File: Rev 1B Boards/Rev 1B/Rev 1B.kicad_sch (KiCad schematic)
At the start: 32 parts, among them J1 JST4_F, J10 Conn_01x01_Pin, J11 Conn_01x01_Pin, J12 Conn_01x01_Pin, J13 Banana 2P, J14 Conn_01x01_Pin, J15 Banana 2P, J16 Conn_01x01_Pin, J17 Conn_01x01_Pin, J18 Banana 2P, J19 Banana 2P, J2 Banana 2P, J21 Banana 2P, J22 Banana 2P, J23 Banana 2P, J24 Banana 2P, J25 Banana 2P, J26 Banana 2P, J27 Banana 2P, J28 Banana 2P, J29 Banana 2P, J3 Banana 2P, J30 Banana 2P, J31 Banana 2P, J4 Banana 2P, J5 Banana 2P, J6 Banana 2P, J7 Conn_01x01_Pin, Q1 BSC059N04LS6, Q2 BSC059N04LS6

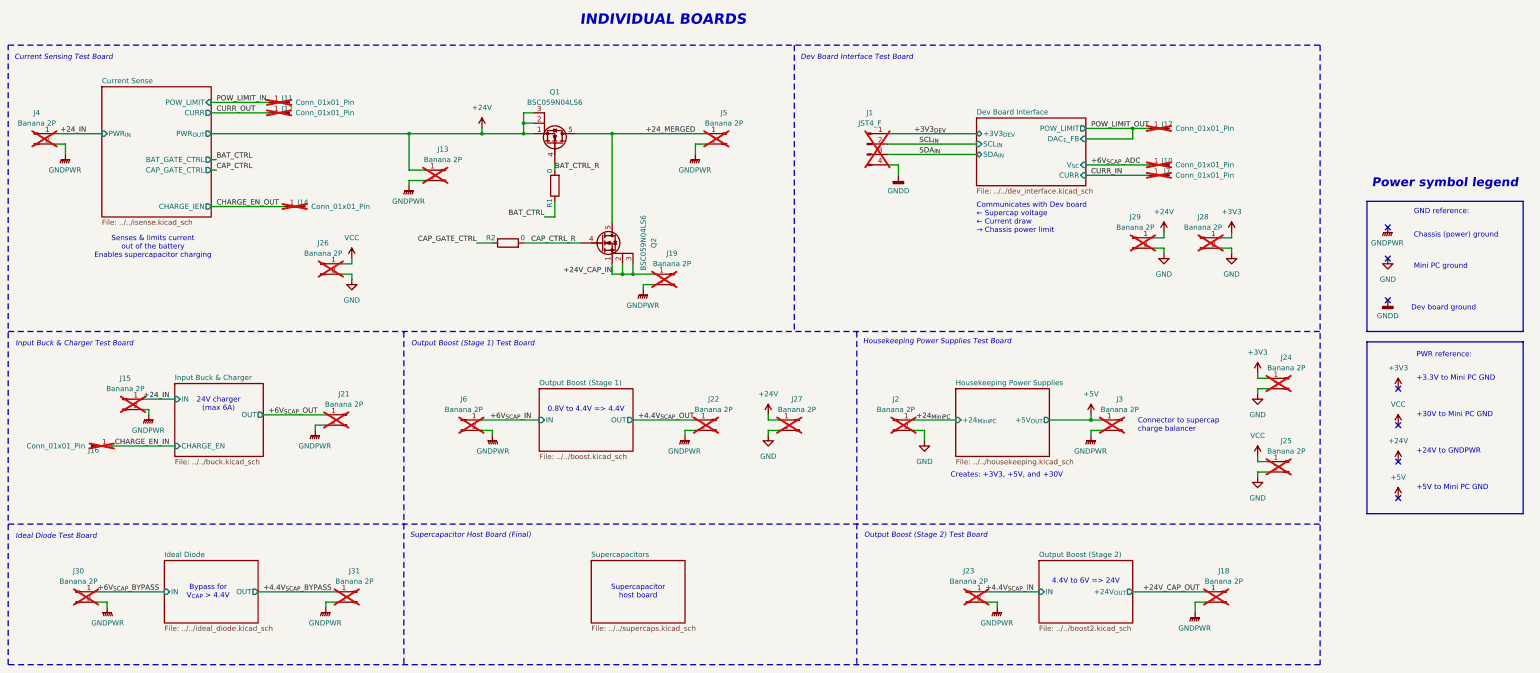
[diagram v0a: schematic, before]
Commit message: Renumbered components for rev 1b layout
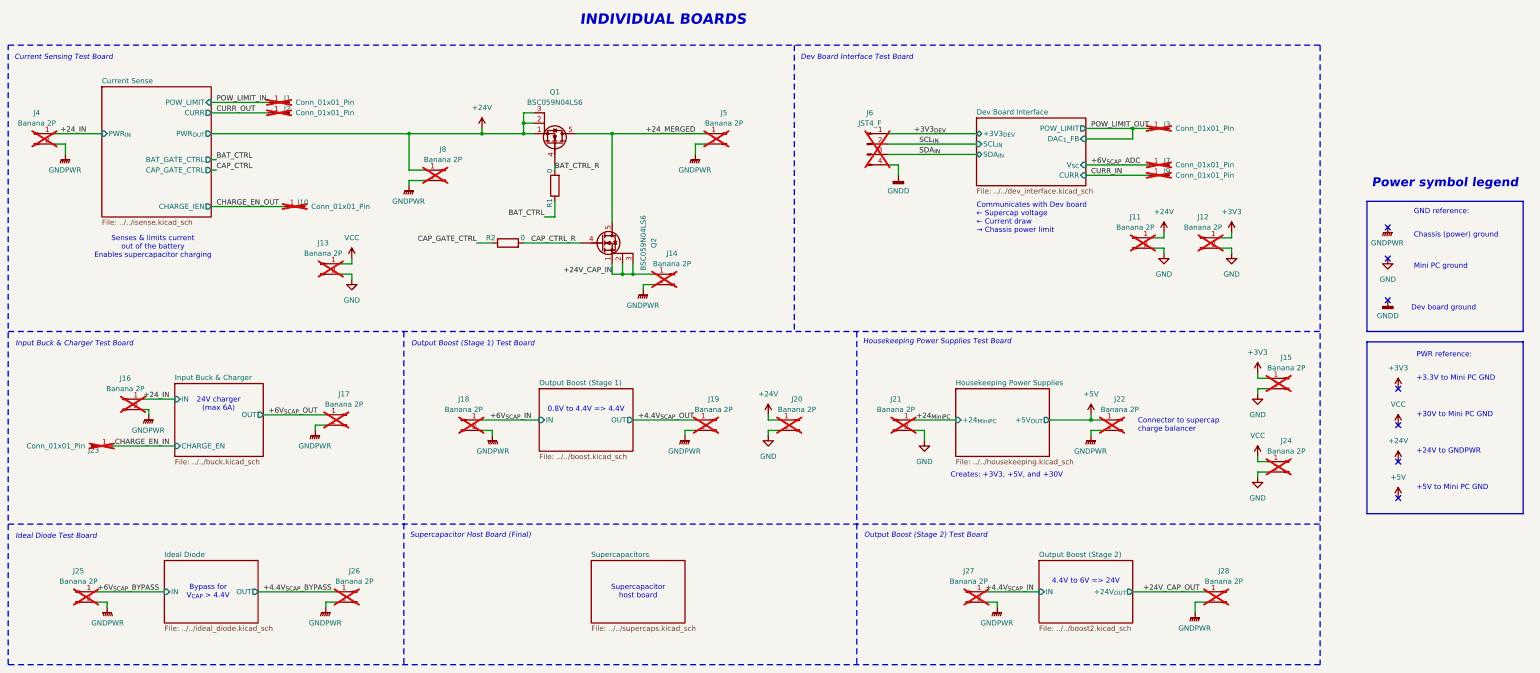
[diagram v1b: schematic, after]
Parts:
- renumbered J11 to J1, J14 to J10, J29 to J11, J28 to J12, J26 to J13, J19 to J14, J24 to J15, J15 to J16, J21 to J17, J6 to J18, J22 to J19, J12 to J2, J27 to J20, J2 to J21, J3 to J22, J16 to J23, J25 to J24, J30 to J25, J31 to J26, J23 to J27, J18 to J28, J17 to J3, J1 to J6, J10 to J7, J13 to J8, J7 to J9
